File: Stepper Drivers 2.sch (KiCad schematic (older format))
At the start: 88 parts

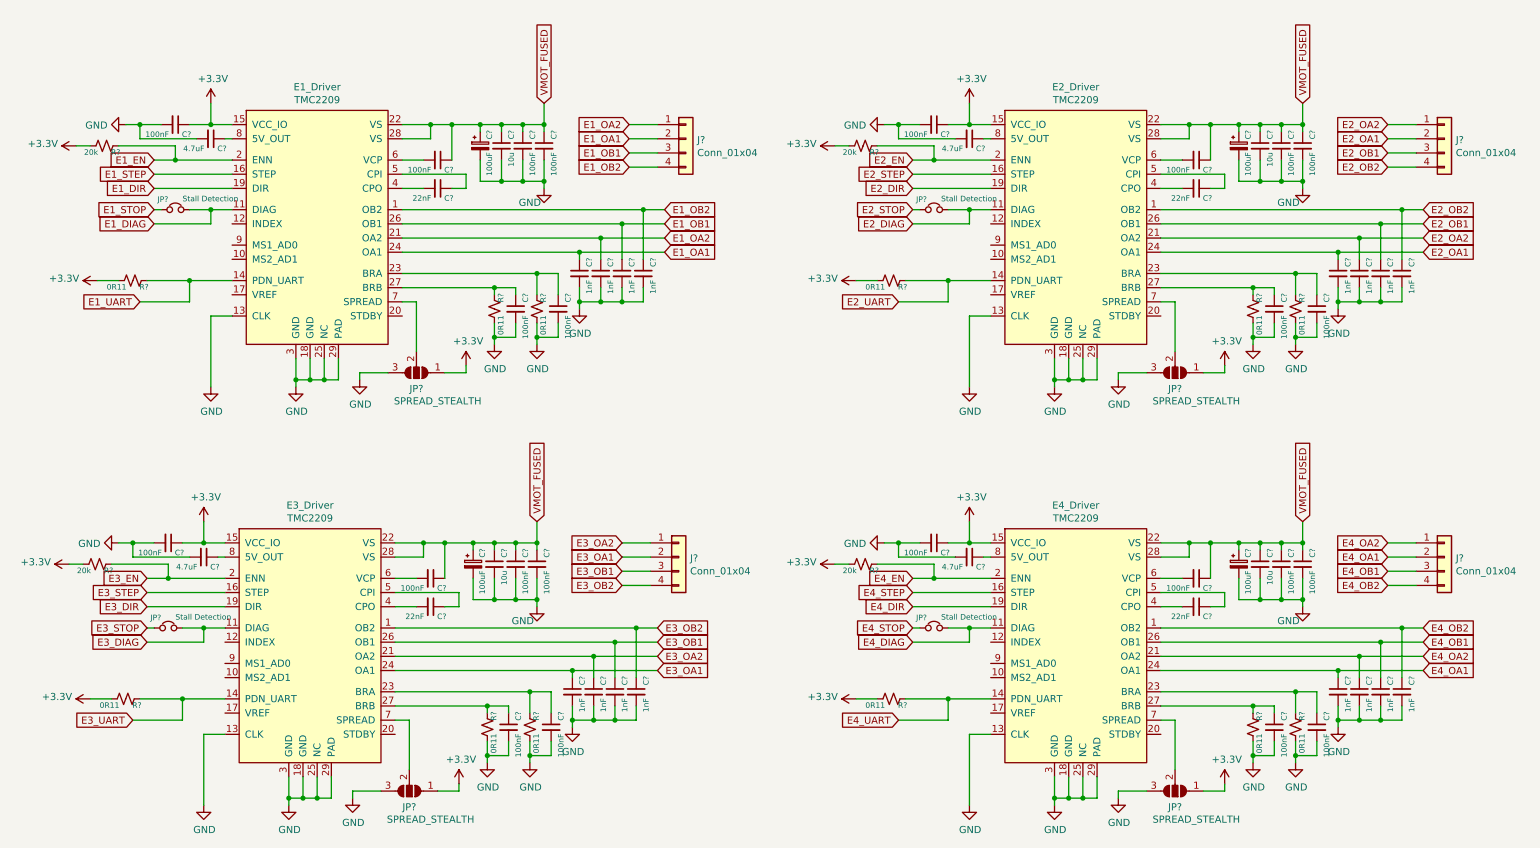
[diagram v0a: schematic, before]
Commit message: added resistor numbers
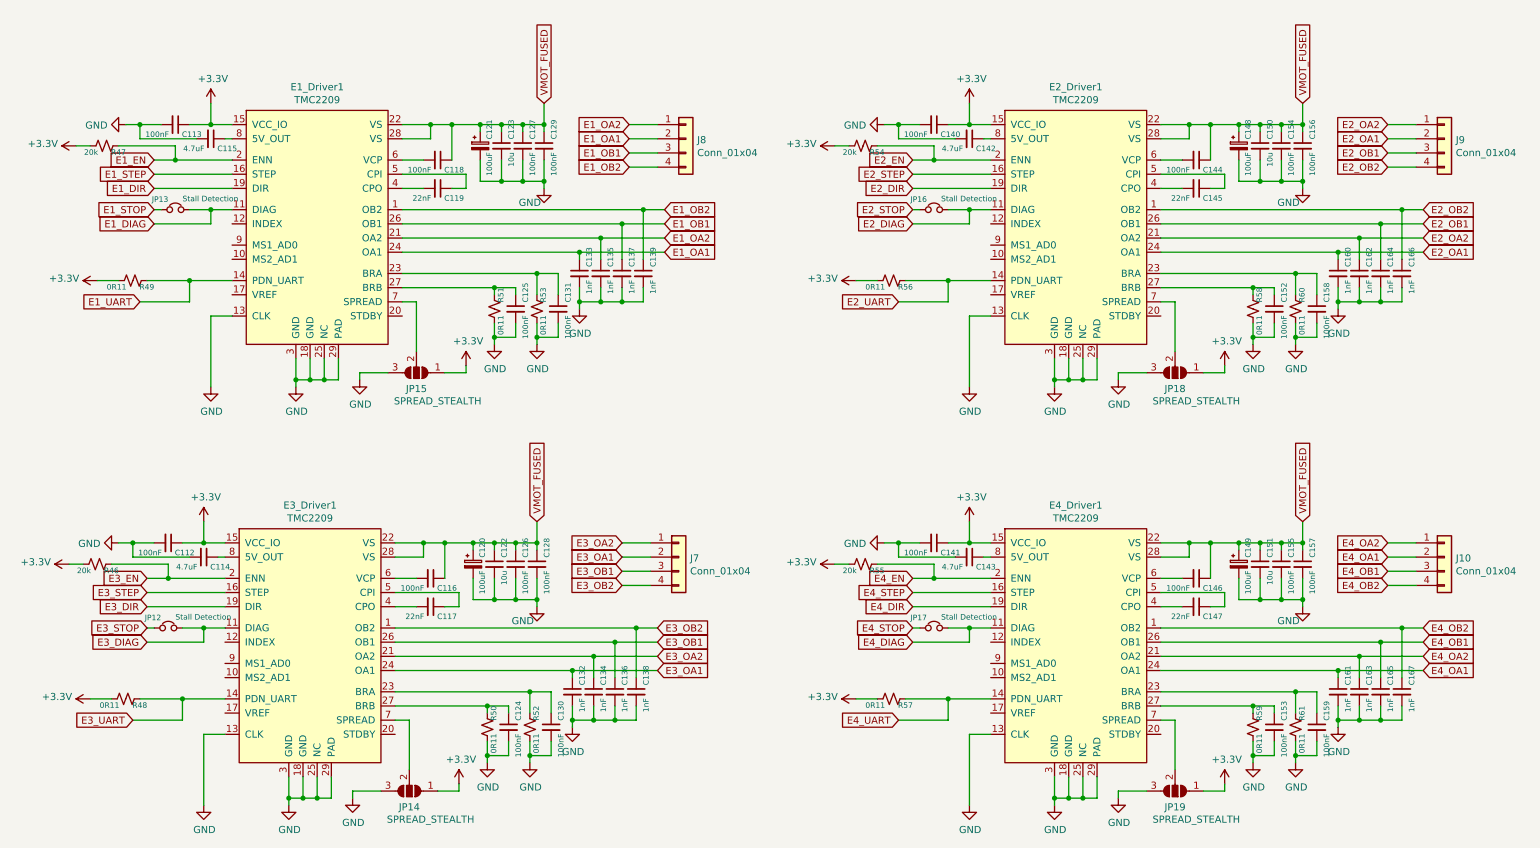
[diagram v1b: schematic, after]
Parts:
- gave numbers to parts that had none: 84
- renumbered E1_Driver to E1_Driver1, E2_Driver to E2_Driver1, E3_Driver to E3_Driver1, E4_Driver to E4_Driver1

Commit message: added raspberry pi header
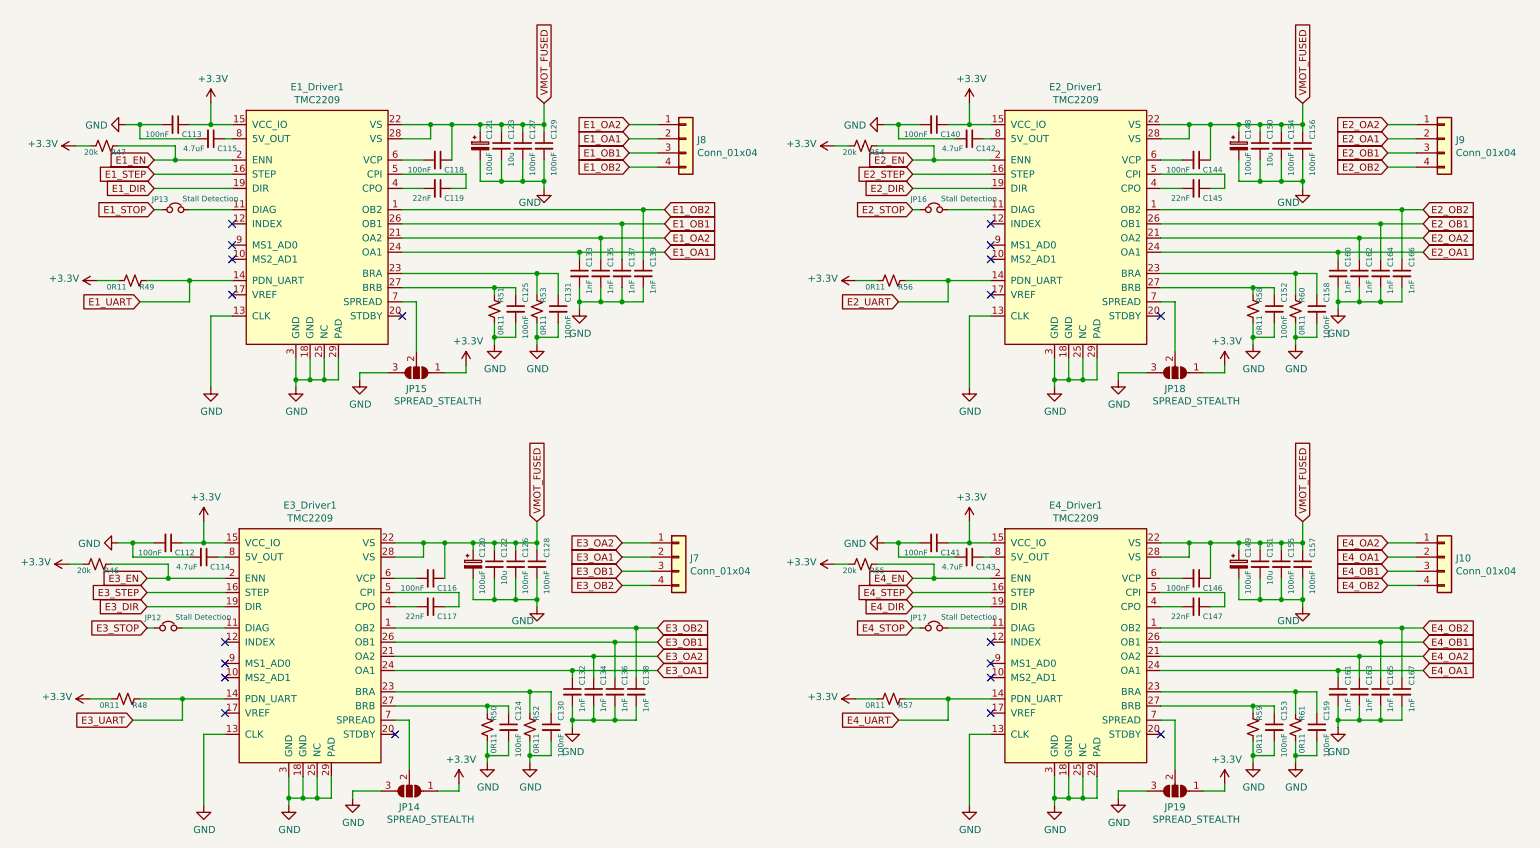
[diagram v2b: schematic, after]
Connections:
- net E1_DIAG: no longer names the net of E1_Driver1.11 (DIAG), JP13.2
- net E2_DIAG: no longer names the net of E2_Driver1.11 (DIAG), JP16.2
- net E3_DIAG: no longer names the net of E3_Driver1.11 (DIAG), JP12.2
- net E4_DIAG: no longer names the net of E4_Driver1.11 (DIAG), JP17.2
- no-connect marks 0 -> 20
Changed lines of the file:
@@
 $EndComp
-Wire Wire Line
-	1500 2000 1900 2000
-Wire Wire Line
-	1900 2000 1900 1900
-Wire Wire Line
-	1900 1900 2050 1900
 Wire Wire Line
 	1500 1900 1550 1900
-Wire Wire Line
-	1750 1900 1900 1900
-Connection ~ 1900 1900
 $Comp
 L Device:C_Small C?
@@
 $EndComp
 Wire Wire Line
-	6850 2000 7250 2000
-Wire Wire Line
-	7250 2000 7250 1900
-Wire Wire Line
-	7250 1900 7400 1900
-Wire Wire Line
 	6850 1900 6900 1900
-Wire Wire Line
-	7100 1900 7250 1900
-Connection ~ 7250 1900
 $Comp
 L Device:C_Small C?
@@
 $EndComp
 Wire Wire Line
-	1450 4950 1850 4950
-Wire Wire Line
-	1850 4950 1850 4850
-Wire Wire Line
-	1850 4850 2000 4850
-Wire Wire Line
 	1450 4850 1500 4850
-Wire Wire Line
-	1700 4850 1850 4850
-Connection ~ 1850 4850
 $Comp
 L Device:C_Small C?
@@
 $EndComp
 Wire Wire Line
-	6850 4950 7250 4950
-Wire Wire Line
-	7250 4950 7250 4850
-Wire Wire Line
-	7250 4850 7400 4850
-Wire Wire Line
 	6850 4850 6900 4850
-Wire Wire Line
-	7100 4850 7250 4850
-Connection ~ 7250 4850
 $Comp
 L Device:C_Small C?
@@
 Text GLabel 1500 1900 0    50   Input ~ 0
 E1_STOP
-Text GLabel 1500 2000 0    50   Input ~ 0
-E1_DIAG
 Text GLabel 1400 2550 0    50   Input ~ 0
 E1_UART
@@
 Text GLabel 6850 1900 0    50   Input ~ 0
 E2_STOP
-Text GLabel 6850 2000 0    50   Input ~ 0
-E2_DIAG
 Text GLabel 6750 2550 0    50   Input ~ 0
 E2_UART
@@
 Text GLabel 1450 4850 0    50   Input ~ 0
 E3_STOP
-Text GLabel 1450 4950 0    50   Input ~ 0
-E3_DIAG
 Text GLabel 1350 5500 0    50   Input ~ 0
 E3_UART
@@
 Text GLabel 6850 4850 0    50   Input ~ 0
 E4_STOP
-Text GLabel 6850 4950 0    50   Input ~ 0
-E4_DIAG
 Text GLabel 6750 5500 0    50   Input ~ 0
 E4_UART
+NoConn ~ 2050 2000
+NoConn ~ 2050 2150
+NoConn ~ 2050 2250
+NoConn ~ 2050 2500
+NoConn ~ 3250 2650
+NoConn ~ 7400 2000
+NoConn ~ 7400 2150
+NoConn ~ 7400 2250
+NoConn ~ 7400 2500
+NoConn ~ 8600 2650
+NoConn ~ 2000 4950
+NoConn ~ 2000 5100
+NoConn ~ 2000 5200
+NoConn ~ 2000 5450
+NoConn ~ 3200 5600
+NoConn ~ 7400 4950
+NoConn ~ 7400 5100
+NoConn ~ 7400 5200
+NoConn ~ 7400 5450
+NoConn ~ 8600 5600
+Wire Wire Line
+	1750 1900 2050 1900
+Wire Wire Line
+	1700 4850 2000 4850
+Wire Wire Line
+	7100 4850 7400 4850
+Wire Wire Line
+	7100 1900 7400 1900
 $EndSCHEMATC

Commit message: assigned some footprints
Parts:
- C112, C113, C116, C118, C124, C125, C126, C127, C128, C129, C130, C131, C140, C141, C144, C146, C152, C153, C154, C155, C156, C157, C158, C159: footprint (none) -> Capacitor_SMD:C_0603_1608Metric_Pad1.05x0.95mm_HandSolder
- C122, C123, C150, C151: footprint (none) -> Capacitor_SMD:C_0805_2012Metric_Pad1.15x1.40mm_HandSolder
- C148, C149: footprint (none) -> Capacitor_SMD:CP_Elec_6.3x7.7
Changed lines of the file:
@@
 F 0 "C123" V 4042 1496 39  0000 L BNN
 F 1 "10u" V 4042 1405 39  0000 R BNN
-F 2 "" H 3950 1450 50  0001 C CNN
+F 2 "Capacitor_SMD:C_0805_2012Metric_Pad1.15x1.40mm_HandSolder" H 3950 1450 50  0001 C CNN
 F 3 "~" H 3950 1450 50  0001 C CNN
 	1    3950 1450
@@
 F 0 "C129" V 4342 1496 39  0000 L BNN
 F 1 "100nF" V 4342 1405 39  0000 R BNN
-F 2 "" H 4250 1450 50  0001 C CNN
+F 2 "Capacitor_SMD:C_0603_1608Metric_Pad1.05x0.95mm_HandSolder" H 4250 1450 50  0001 C CNN
 F 3 "~" H 4250 1450 50  0001 C CNN
 	1    4250 1450
@@
 F 0 "C127" V 4192 1496 39  0000 L BNN
 F 1 "100nF" V 4192 1405 39  0000 R BNN
-F 2 "" H 4100 1450 50  0001 C CNN
+F 2 "Capacitor_SMD:C_0603_1608Metric_Pad1.05x0.95mm_HandSolder" H 4100 1450 50  0001 C CNN
 F 3 "~" H 4100 1450 50  0001 C CNN
 	1    4100 1450
@@
 F 0 "C118" V 3592 1596 39  0000 L BNN
 F 1 "100nF" V 3592 1505 39  0000 R BNN
-F 2 "" H 3500 1550 50  0001 C CNN
+F 2 "Capacitor_SMD:C_0603_1608Metric_Pad1.05x0.95mm_HandSolder" H 3500 1550 50  0001 C CNN
 F 3 "~" H 3500 1550 50  0001 C CNN
 	1    3500 1550
@@
 F 0 "C113" V 1742 1346 39  0000 L BNN
 F 1 "100nF" V 1742 1255 39  0000 R BNN
-F 2 "" H 1650 1300 50  0001 C CNN
+F 2 "Capacitor_SMD:C_0603_1608Metric_Pad1.05x0.95mm_HandSolder" H 1650 1300 50  0001 C CNN
 F 3 "~" H 1650 1300 50  0001 C CNN
 	1    1650 1300
@@
 F 0 "C131" V 4442 2646 39  0000 L BNN
 F 1 "100nF" V 4442 2555 39  0000 R BNN
-F 2 "" H 4350 2600 50  0001 C CNN
+F 2 "Capacitor_SMD:C_0603_1608Metric_Pad1.05x0.95mm_HandSolder" H 4350 2600 50  0001 C CNN
 F 3 "~" H 4350 2600 50  0001 C CNN
 	1    4350 2600
@@
 F 0 "C125" V 4142 2646 39  0000 L BNN
 F 1 "100nF" V 4142 2555 39  0000 R BNN
-F 2 "" H 4050 2600 50  0001 C CNN
+F 2 "Capacitor_SMD:C_0603_1608Metric_Pad1.05x0.95mm_HandSolder" H 4050 2600 50  0001 C CNN
 F 3 "~" H 4050 2600 50  0001 C CNN
 	1    4050 2600
@@
 F 0 "C148" V 9238 1496 39  0000 L BNN
 F 1 "100uF" V 9238 1405 39  0000 R BNN
-F 2 "" H 9150 1450 50  0001 C CNN
+F 2 "Capacitor_SMD:CP_Elec_6.3x7.7" H 9150 1450 50  0001 C CNN
 F 3 "~" H 9150 1450 50  0001 C CNN
 	1    9150 1450
@@
 F 0 "C150" V 9392 1496 39  0000 L BNN
 F 1 "10u" V 9392 1405 39  0000 R BNN
-F 2 "" H 9300 1450 50  0001 C CNN
+F 2 "Capacitor_SMD:C_0805_2012Metric_Pad1.15x1.40mm_HandSolder" H 9300 1450 50  0001 C CNN
 F 3 "~" H 9300 1450 50  0001 C CNN
 	1    9300 1450
@@
 F 0 "C156" V 9692 1496 39  0000 L BNN
 F 1 "100nF" V 9692 1405 39  0000 R BNN
-F 2 "" H 9600 1450 50  0001 C CNN
+F 2 "Capacitor_SMD:C_0603_1608Metric_Pad1.05x0.95mm_HandSolder" H 9600 1450 50  0001 C CNN
 F 3 "~" H 9600 1450 50  0001 C CNN
 	1    9600 1450
@@
 F 0 "C154" V 9542 1496 39  0000 L BNN
 F 1 "100nF" V 9542 1405 39  0000 R BNN
-F 2 "" H 9450 1450 50  0001 C CNN
+F 2 "Capacitor_SMD:C_0603_1608Metric_Pad1.05x0.95mm_HandSolder" H 9450 1450 50  0001 C CNN
 F 3 "~" H 9450 1450 50  0001 C CNN
 	1    9450 1450
@@
 F 0 "C144" V 8942 1596 39  0000 L BNN
 F 1 "100nF" V 8942 1505 39  0000 R BNN
-F 2 "" H 8850 1550 50  0001 C CNN
+F 2 "Capacitor_SMD:C_0603_1608Metric_Pad1.05x0.95mm_HandSolder" H 8850 1550 50  0001 C CNN
 F 3 "~" H 8850 1550 50  0001 C CNN
 	1    8850 1550
@@
 F 0 "C140" V 7092 1346 39  0000 L BNN
 F 1 "100nF" V 7092 1255 39  0000 R BNN
-F 2 "" H 7000 1300 50  0001 C CNN
+F 2 "Capacitor_SMD:C_0603_1608Metric_Pad1.05x0.95mm_HandSolder" H 7000 1300 50  0001 C CNN
 F 3 "~" H 7000 1300 50  0001 C CNN
 	1    7000 1300
@@
 F 0 "C158" V 9792 2646 39  0000 L BNN
 F 1 "100nF" V 9792 2555 39  0000 R BNN
-F 2 "" H 9700 2600 50  0001 C CNN
+F 2 "Capacitor_SMD:C_0603_1608Metric_Pad1.05x0.95mm_HandSolder" H 9700 2600 50  0001 C CNN
 F 3 "~" H 9700 2600 50  0001 C CNN
 	1    9700 2600
@@
 F 0 "C152" V 9492 2646 39  0000 L BNN
 F 1 "100nF" V 9492 2555 39  0000 R BNN
-F 2 "" H 9400 2600 50  0001 C CNN
+F 2 "Capacitor_SMD:C_0603_1608Metric_Pad1.05x0.95mm_HandSolder" H 9400 2600 50  0001 C CNN
 F 3 "~" H 9400 2600 50  0001 C CNN
 	1    9400 2600
@@
 F 0 "C122" V 3992 4446 39  0000 L BNN
 F 1 "10u" V 3992 4355 39  0000 R BNN
-F 2 "" H 3900 4400 50  0001 C CNN
+F 2 "Capacitor_SMD:C_0805_2012Metric_Pad1.15x1.40mm_HandSolder" H 3900 4400 50  0001 C CNN
 F 3 "~" H 3900 4400 50  0001 C CNN
 	1    3900 4400
@@
 F 0 "C128" V 4292 4446 39  0000 L BNN
 F 1 "100nF" V 4292 4355 39  0000 R BNN
-F 2 "" H 4200 4400 50  0001 C CNN
+F 2 "Capacitor_SMD:C_0603_1608Metric_Pad1.05x0.95mm_HandSolder" H 4200 4400 50  0001 C CNN
 F 3 "~" H 4200 4400 50  0001 C CNN
 	1    4200 4400
@@
 F 0 "C126" V 4142 4446 39  0000 L BNN
 F 1 "100nF" V 4142 4355 39  0000 R BNN
-F 2 "" H 4050 4400 50  0001 C CNN
+F 2 "Capacitor_SMD:C_0603_1608Metric_Pad1.05x0.95mm_HandSolder" H 4050 4400 50  0001 C CNN
 F 3 "~" H 4050 4400 50  0001 C CNN
 	1    4050 4400
@@
 F 0 "C116" V 3542 4546 39  0000 L BNN
 F 1 "100nF" V 3542 4455 39  0000 R BNN
-F 2 "" H 3450 4500 50  0001 C CNN
+F 2 "Capacitor_SMD:C_0603_1608Metric_Pad1.05x0.95mm_HandSolder" H 3450 4500 50  0001 C CNN
 F 3 "~" H 3450 4500 50  0001 C CNN
 	1    3450 4500
@@
 F 0 "C112" V 1692 4296 39  0000 L BNN
 F 1 "100nF" V 1692 4205 39  0000 R BNN
-F 2 "" H 1600 4250 50  0001 C CNN
+F 2 "Capacitor_SMD:C_0603_1608Metric_Pad1.05x0.95mm_HandSolder" H 1600 4250 50  0001 C CNN
 F 3 "~" H 1600 4250 50  0001 C CNN
 	1    1600 4250
@@
 F 0 "C130" V 4392 5596 39  0000 L BNN
 F 1 "100nF" V 4392 5505 39  0000 R BNN
-F 2 "" H 4300 5550 50  0001 C CNN
+F 2 "Capacitor_SMD:C_0603_1608Metric_Pad1.05x0.95mm_HandSolder" H 4300 5550 50  0001 C CNN
 F 3 "~" H 4300 5550 50  0001 C CNN
 	1    4300 5550
@@
 F 0 "C124" V 4092 5596 39  0000 L BNN
 F 1 "100nF" V 4092 5505 39  0000 R BNN
-F 2 "" H 4000 5550 50  0001 C CNN
+F 2 "Capacitor_SMD:C_0603_1608Metric_Pad1.05x0.95mm_HandSolder" H 4000 5550 50  0001 C CNN
 F 3 "~" H 4000 5550 50  0001 C CNN
 	1    4000 5550
@@
 F 0 "C149" V 9238 4446 39  0000 L BNN
 F 1 "100uF" V 9238 4355 39  0000 R BNN
-F 2 "" H 9150 4400 50  0001 C CNN
+F 2 "Capacitor_SMD:CP_Elec_6.3x7.7" H 9150 4400 50  0001 C CNN
 F 3 "~" H 9150 4400 50  0001 C CNN
 	1    9150 4400
@@
 F 0 "C151" V 9392 4446 39  0000 L BNN
 F 1 "10u" V 9392 4355 39  0000 R BNN
-F 2 "" H 9300 4400 50  0001 C CNN
+F 2 "Capacitor_SMD:C_0805_2012Metric_Pad1.15x1.40mm_HandSolder" H 9300 4400 50  0001 C CNN
 F 3 "~" H 9300 4400 50  0001 C CNN
 	1    9300 4400
@@
 F 0 "C157" V 9692 4446 39  0000 L BNN
 F 1 "100nF" V 9692 4355 39  0000 R BNN
-F 2 "" H 9600 4400 50  0001 C CNN
+F 2 "Capacitor_SMD:C_0603_1608Metric_Pad1.05x0.95mm_HandSolder" H 9600 4400 50  0001 C CNN
 F 3 "~" H 9600 4400 50  0001 C CNN
 	1    9600 4400
@@
 F 0 "C155" V 9542 4446 39  0000 L BNN
 F 1 "100nF" V 9542 4355 39  0000 R BNN
-F 2 "" H 9450 4400 50  0001 C CNN
+F 2 "Capacitor_SMD:C_0603_1608Metric_Pad1.05x0.95mm_HandSolder" H 9450 4400 50  0001 C CNN
 F 3 "~" H 9450 4400 50  0001 C CNN
 	1    9450 4400
@@
 F 0 "C146" V 8942 4546 39  0000 L BNN
 F 1 "100nF" V 8942 4455 39  0000 R BNN
-F 2 "" H 8850 4500 50  0001 C CNN
+F 2 "Capacitor_SMD:C_0603_1608Metric_Pad1.05x0.95mm_HandSolder" H 8850 4500 50  0001 C CNN
 F 3 "~" H 8850 4500 50  0001 C CNN
 	1    8850 4500
@@
 F 0 "C141" V 7092 4296 39  0000 L BNN
 F 1 "100nF" V 7092 4205 39  0000 R BNN
-F 2 "" H 7000 4250 50  0001 C CNN
+F 2 "Capacitor_SMD:C_0603_1608Metric_Pad1.05x0.95mm_HandSolder" H 7000 4250 50  0001 C CNN
 F 3 "~" H 7000 4250 50  0001 C CNN
 	1    7000 4250
@@
 F 0 "C159" V 9792 5596 39  0000 L BNN
 F 1 "100nF" V 9792 5505 39  0000 R BNN
-F 2 "" H 9700 5550 50  0001 C CNN
+F 2 "Capacitor_SMD:C_0603_1608Metric_Pad1.05x0.95mm_HandSolder" H 9700 5550 50  0001 C CNN
 F 3 "~" H 9700 5550 50  0001 C CNN
 	1    9700 5550
@@
 F 0 "C153" V 9492 5596 39  0000 L BNN
 F 1 "100nF" V 9492 5505 39  0000 R BNN
-F 2 "" H 9400 5550 50  0001 C CNN
+F 2 "Capacitor_SMD:C_0603_1608Metric_Pad1.05x0.95mm_HandSolder" H 9400 5550 50  0001 C CNN
 F 3 "~" H 9400 5550 50  0001 C CNN
 	1    9400 5550

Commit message: associated more footprints
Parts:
- C114, C115, C142, C143: footprint (none) -> Capacitor_SMD:C_0805_2012Metric_Pad1.15x1.40mm_HandSolder
- C117, C119, C132, C133, C134, C135, C136, C137, C138, C139, C145, C147, C160, C161, C162, C163, C164, C165, C166, C167: footprint (none) -> Capacitor_SMD:C_0603_1608Metric_Pad1.05x0.95mm_HandSolder
- C120, C121: footprint (none) -> Capacitor_SMD:CP_Elec_6.3x7.7
- J10, J7, J8, J9: footprint (none) -> Connector_Molex:Molex_KK-254_AE-6410-04A_1x04_P2.54mm_Vertical
- JP12, JP13, JP16, JP17: footprint (none) -> Connector_PinHeader_2.54mm:PinHeader_1x02_P2.54mm_Vertical
- JP14, JP15, JP18, JP19: footprint (none) -> Connector_PinHeader_2.54mm:PinHeader_1x03_P2.54mm_Vertical
